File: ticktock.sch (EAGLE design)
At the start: 64 parts, among them IC1 ATMEGA644A, IC2 AD8611RM, IC3 REF200U, J1 AVR_SPI_PRG_6NS, Q1 MOSFET-NCHANNEL2N7002PW, Q2 MOSFET-NCHANNELBSS138, Q3 MOSFET-NCHANNELBSS138, U1 MAX232SOIC16, U2 OSCILLATORSMD, U3 FT232RLSSOP, U4 BMP180

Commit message: Fix ERC and DRC complaints.  Connect accidentally unconnected nets.
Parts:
- JP2: value (none) -> 3 Pin
- JP8: value (none) -> 7-Pin
- JP9: value (none) -> 3-Pin
- U$1: value (none) -> OPA381
- X1: value (none) -> RS232
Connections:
- net GND: now also U$1.IN+, U$1.V-

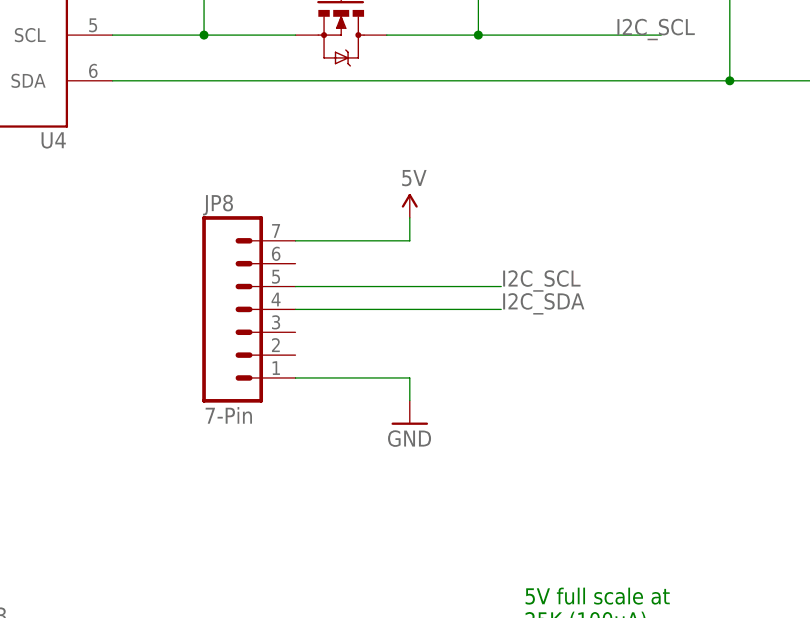
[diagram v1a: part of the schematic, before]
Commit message: Remove BMP carrier board header and Pull RS232 connector back to PCB edge
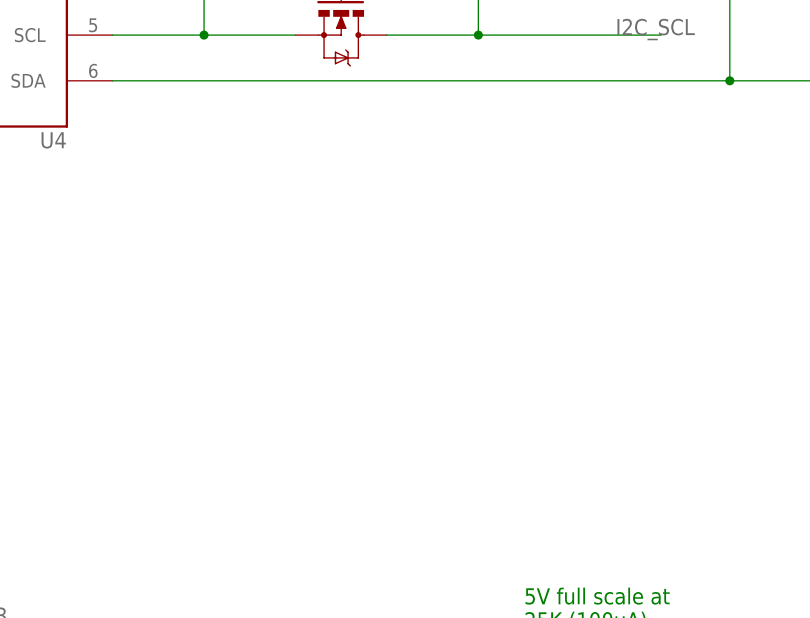
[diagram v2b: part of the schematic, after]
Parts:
- removed JP8: 7-Pin, SparkFun-Connectors:M07LOCK
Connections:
- net 5V: no longer JP8.7
- net GND: no longer JP8.1
- net I2C_SCL: no longer JP8.5
- net I2C_SDA: no longer JP8.4
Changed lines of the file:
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@@
 <part name="JP6" library="SparkFun-Connectors" deviceset="M01" device="PTH"/>
 <part name="JP7" library="SparkFun-Connectors" deviceset="M01" device="PTH"/>
-<part name="JP8" library="SparkFun-Connectors" deviceset="M07" device="LOCK" value="7-Pin"/>
-<part name="SUPPLY31" library="SparkFun-Aesthetics" deviceset="5V" device=""/>
-<part name="GND25" library="SparkFun-Aesthetics" deviceset="GND" device=""/>
 <part name="STANDOFF1" library="SparkFun-Electromechanical" deviceset="STAND-OFF" device=""/>
 <part name="STANDOFF2" library="SparkFun-Electromechanical" deviceset="STAND-OFF" device=""/>
@@
 <instance part="JP6" gate="G$1" x="200.66" y="198.12" rot="R270"/>
 <instance part="JP7" gate="G$1" x="190.5" y="198.12" rot="R270"/>
-<instance part="JP8" gate="G$1" x="403.86" y="111.76"/>
-<instance part="SUPPLY31" gate="G$1" x="421.64" y="124.46"/>
-<instance part="GND25" gate="1" x="421.64" y="101.6"/>
 <instance part="STANDOFF1" gate="G$1" x="487.68" y="307.34"/>
 <instance part="STANDOFF2" gate="G$1" x="487.68" y="302.26"/>
@@
 </segment>
 <segment>
-<pinref part="JP8" gate="G$1" pin="1"/>
-<wire x1="408.94" y1="106.68" x2="421.64" y2="106.68" width="0.1524" layer="91"/>
-<pinref part="GND25" gate="1" pin="GND"/>
-<wire x1="421.64" y1="106.68" x2="421.64" y2="104.14" width="0.1524" layer="91"/>
-</segment>
-<segment>
 <pinref part="U$1" gate="G$1" pin="IN+"/>
 <pinref part="GND21" gate="1" pin="GND"/>
@@
 <pinref part="SUPPLY27" gate="G$1" pin="5V"/>
 <wire x1="487.68" y1="160.02" x2="487.68" y2="180.34" width="0.1524" layer="91"/>
-</segment>
-<segment>
-<pinref part="JP8" gate="G$1" pin="7"/>
-<wire x1="408.94" y1="121.92" x2="421.64" y2="121.92" width="0.1524" layer="91"/>
-<pinref part="SUPPLY31" gate="G$1" pin="5V"/>
-<wire x1="421.64" y1="121.92" x2="421.64" y2="124.46" width="0.1524" layer="91"/>
 </segment>
 <segment>
@@
 <label x="187.96" y="124.46" size="1.778" layer="95"/>
 </segment>
-<segment>
-<pinref part="JP8" gate="G$1" pin="5"/>
-<wire x1="408.94" y1="116.84" x2="431.8" y2="116.84" width="0.1524" layer="91"/>
-<label x="431.8" y="116.84" size="1.778" layer="95"/>
-</segment>
 </net>
 <net name="N$18" class="0">
@@
 <label x="187.96" y="127" size="1.778" layer="95"/>
 </segment>
-<segment>
-<pinref part="JP8" gate="G$1" pin="4"/>
-<wire x1="408.94" y1="114.3" x2="431.8" y2="114.3" width="0.1524" layer="91"/>
-<label x="431.8" y="114.3" size="1.778" layer="95"/>
-</segment>
-</net>
+</net>

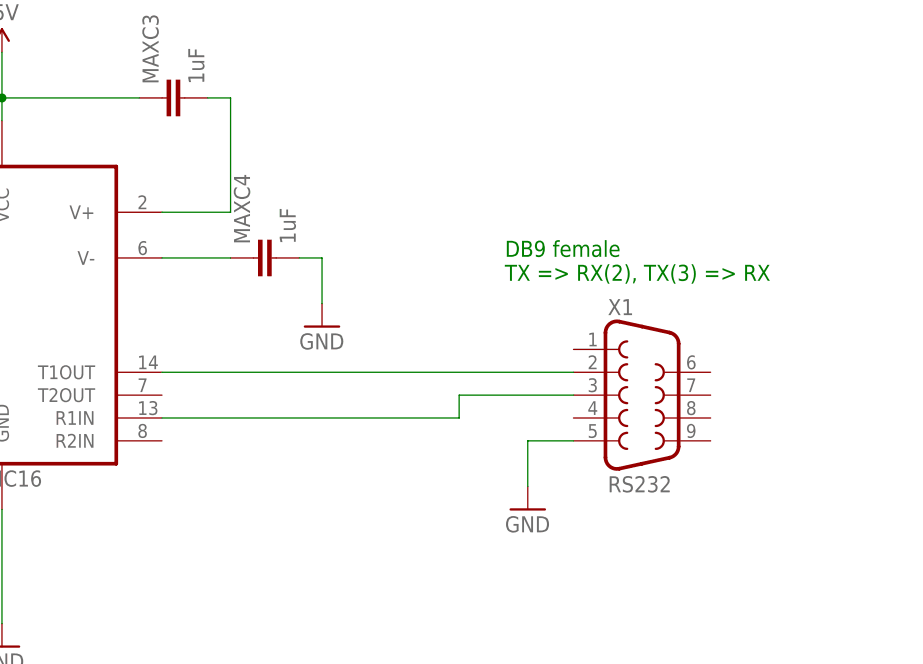
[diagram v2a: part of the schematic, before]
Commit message: Replace DB9 female connector with a male one
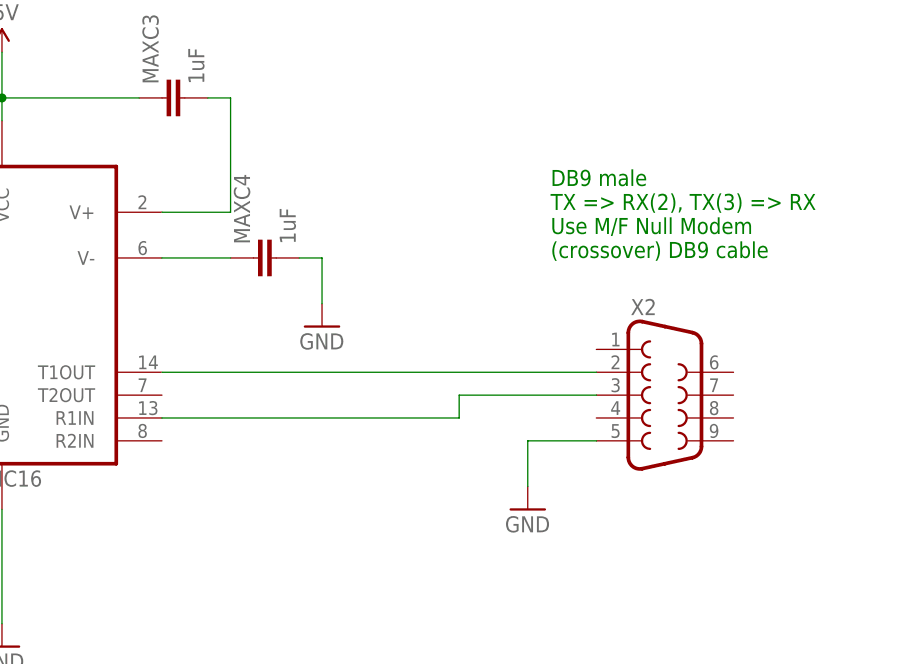
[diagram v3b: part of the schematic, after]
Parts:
- removed X1: RS232, SparkFun-Connectors:DB9FEMALE
- added X2: (no value), SparkFun-Connectors:DB9MALE
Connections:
- net GND: now also X2.5; no longer X1.5
- net N$10: now also X2.3; no longer X1.3
- net N$8: now also X2.2; no longer X1.2
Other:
- note added: "DB9 male TX => RX(2), TX(3) => RX Use M/F Null Modem (crossover) DB9 cable"
- note removed: "DB9 female TX => RX(2), TX(3) => RX"
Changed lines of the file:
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@@
 <part name="MAXC4" library="SparkFun-Capacitors" deviceset="CAP" device="0805" value="1uF"/>
 <part name="GND5" library="SparkFun-Aesthetics" deviceset="GND" device=""/>
-<part name="X1" library="SparkFun-Connectors" deviceset="DB9" device="FEMALE" value="RS232"/>
 <part name="GND6" library="SparkFun-Aesthetics" deviceset="GND" device=""/>
 <part name="GPS_10MHZ_IN" library="SparkFun-Connectors" deviceset="BNC" device="PTH"/>
@@
 <part name="STANDOFF4" library="SparkFun-Electromechanical" deviceset="STAND-OFF" device=""/>
 <part name="JP9" library="SparkFun-Connectors" deviceset="M03" device="LOCK" value="3-Pin"/>
+<part name="X2" library="SparkFun-Connectors" deviceset="DB9" device="MALE"/>
 </parts>
 <sheets>
@@
 <text x="403.86" y="358.14" size="1.778" layer="91">Only using one of the
 MAX232's Rx/Tx pairs</text>
-<text x="510.54" y="388.62" size="1.778" layer="91">DB9 female
+<text x="515.62" y="391.16" size="1.778" layer="91">DB9 male
 TX =&gt; RX(2), TX(3) =&gt; RX
-</text>
+Use M/F Null Modem
+(crossover) DB9 cable</text>
 <text x="20.32" y="40.64" size="1.778" layer="91">USB-B
 (square)</text>
@@
 </instance>
 <instance part="GND5" gate="1" x="490.22" y="383.54"/>
-<instance part="X1" gate="G$1" x="525.78" y="375.92"/>
 <instance part="GND6" gate="1" x="513.08" y="363.22"/>
 <instance part="GPS_10MHZ_IN" gate="G$1" x="307.34" y="327.66"/>
@@
 <instance part="STANDOFF4" gate="G$1" x="487.68" y="292.1"/>
 <instance part="JP9" gate="G$1" x="220.98" y="83.82" rot="R270"/>
+<instance part="X2" gate="G$1" x="528.32" y="375.92"/>
 </instances>
 <busses>
@@
 </segment>
 <segment>
-<pinref part="X1" gate="G$1" pin="5"/>
-<wire x1="518.16" y1="370.84" x2="513.08" y2="370.84" width="0.1524" layer="91"/>
+<wire x1="520.7" y1="370.84" x2="513.08" y2="370.84" width="0.1524" layer="91"/>
 <pinref part="GND6" gate="1" pin="GND"/>
 <wire x1="513.08" y1="370.84" x2="513.08" y2="365.76" width="0.1524" layer="91"/>
+<pinref part="X2" gate="G$1" pin="5"/>
 </segment>
 <segment>
@@
 <segment>
 <pinref part="U1" gate="G$1" pin="T1OUT"/>
-<wire x1="472.44" y1="378.46" x2="518.16" y2="378.46" width="0.1524" layer="91"/>
-<pinref part="X1" gate="G$1" pin="2"/>
+<wire x1="472.44" y1="378.46" x2="520.7" y2="378.46" width="0.1524" layer="91"/>
+<pinref part="X2" gate="G$1" pin="2"/>
 </segment>
 </net>
@@
 <wire x1="472.44" y1="373.38" x2="505.46" y2="373.38" width="0.1524" layer="91"/>
 <wire x1="505.46" y1="373.38" x2="505.46" y2="375.92" width="0.1524" layer="91"/>
-<pinref part="X1" gate="G$1" pin="3"/>
-<wire x1="505.46" y1="375.92" x2="518.16" y2="375.92" width="0.1524" layer="91"/>
-</segment>
-</net>
+<wire x1="505.46" y1="375.92" x2="520.7" y2="375.92" width="0.1524" layer="91"/>
+<pinref part="X2" gate="G$1" pin="3"/>
+</segment>
+</net>

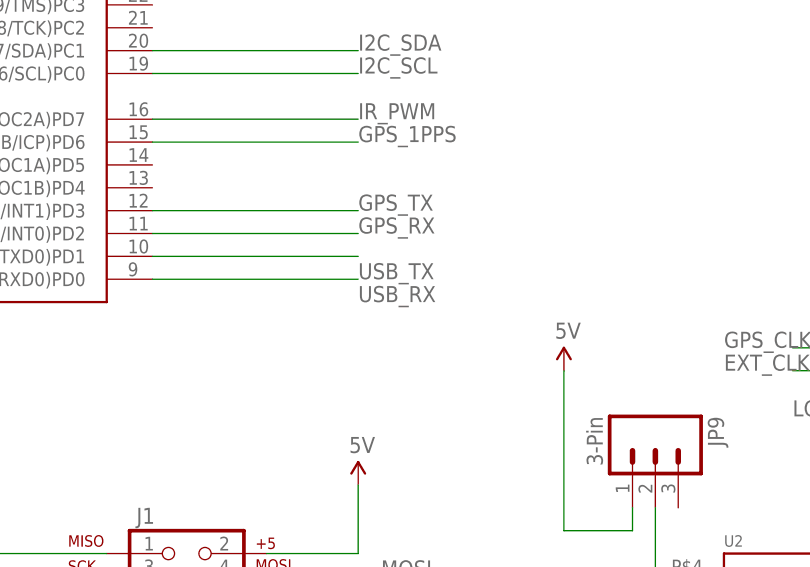
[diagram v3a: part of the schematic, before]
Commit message: Flip USB_TX and USB_RX in schematic
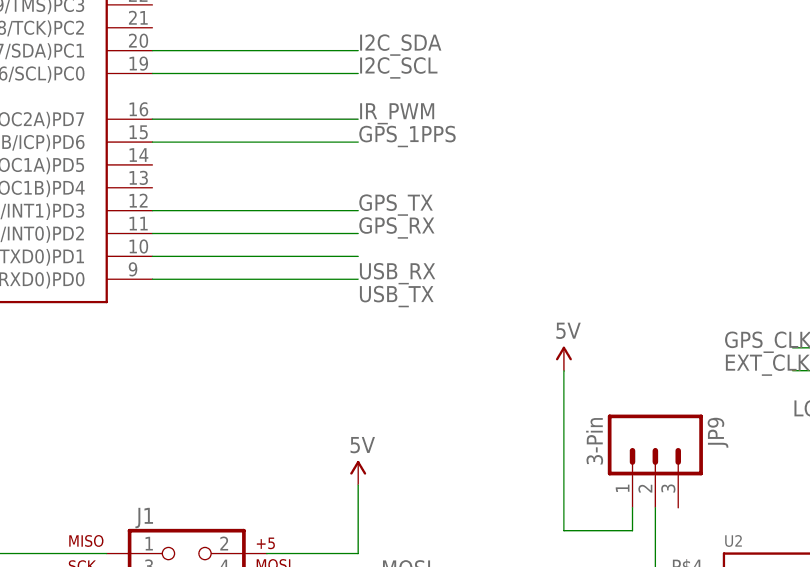
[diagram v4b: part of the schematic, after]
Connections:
- net USB_RX: now also IC1.(PCINT25/TXD0)PD1; no longer IC1.(PCINT24/RXD0)PD0
- net USB_TX: now also IC1.(PCINT24/RXD0)PD0; no longer IC1.(PCINT25/TXD0)PD1
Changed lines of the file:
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@@
+</segment>
+</net>
+<net name="USB_RX" class="0">
+<segment>
+<pinref part="IC1" gate="G$1" pin="(PCINT25/TXD0)PD1"/>
+<wire x1="165.1" y1="104.14" x2="187.96" y2="104.14" width="0.1524" layer="91"/>
+<label x="187.96" y="101.6" size="1.778" layer="95"/>
+</segment>
+<segment>
+<pinref part="U3" gate="G$1" pin="RXD"/>
+<wire x1="88.9" y1="58.42" x2="101.6" y2="58.42" width="0.1524" layer="91"/>
+<label x="101.6" y="58.42" size="1.778" layer="95"/>
 </segment>
 </net>
 <net name="USB_TX" class="0">
+<segment>
+<pinref part="IC1" gate="G$1" pin="(PCINT24/RXD0)PD0"/>
+<wire x1="165.1" y1="101.6" x2="187.96" y2="101.6" width="0.1524" layer="91"/>
+<label x="187.96" y="99.06" size="1.778" layer="95"/>
+</segment>
 <segment>
 <pinref part="U3" gate="G$1" pin="TXD"/>
@@
 <label x="101.6" y="60.96" size="1.778" layer="95"/>
 </segment>
-<segment>
-<pinref part="IC1" gate="G$1" pin="(PCINT25/TXD0)PD1"/>
-<wire x1="165.1" y1="104.14" x2="187.96" y2="104.14" width="0.1524" layer="91"/>
-<label x="187.96" y="101.6" size="1.778" layer="95"/>
-</segment>
 </net>
-<net name="USB_RX" class="0">
-<segment>
-<pinref part="U3" gate="G$1" pin="RXD"/>
-<wire x1="88.9" y1="58.42" x2="101.6" y2="58.42" width="0.1524" layer="91"/>
-<label x="101.6" y="58.42" size="1.778" layer="95"/>
-</segment>
-<segment>
-<pinref part="IC1" gate="G$1" pin="(PCINT24/RXD0)PD0"/>
-<wire x1="165.1" y1="101.6" x2="187.96" y2="101.6" width="0.1524" layer="91"/>
-<label x="187.96" y="99.06" size="1.778" layer="95"/>
-</segment>
-</net>

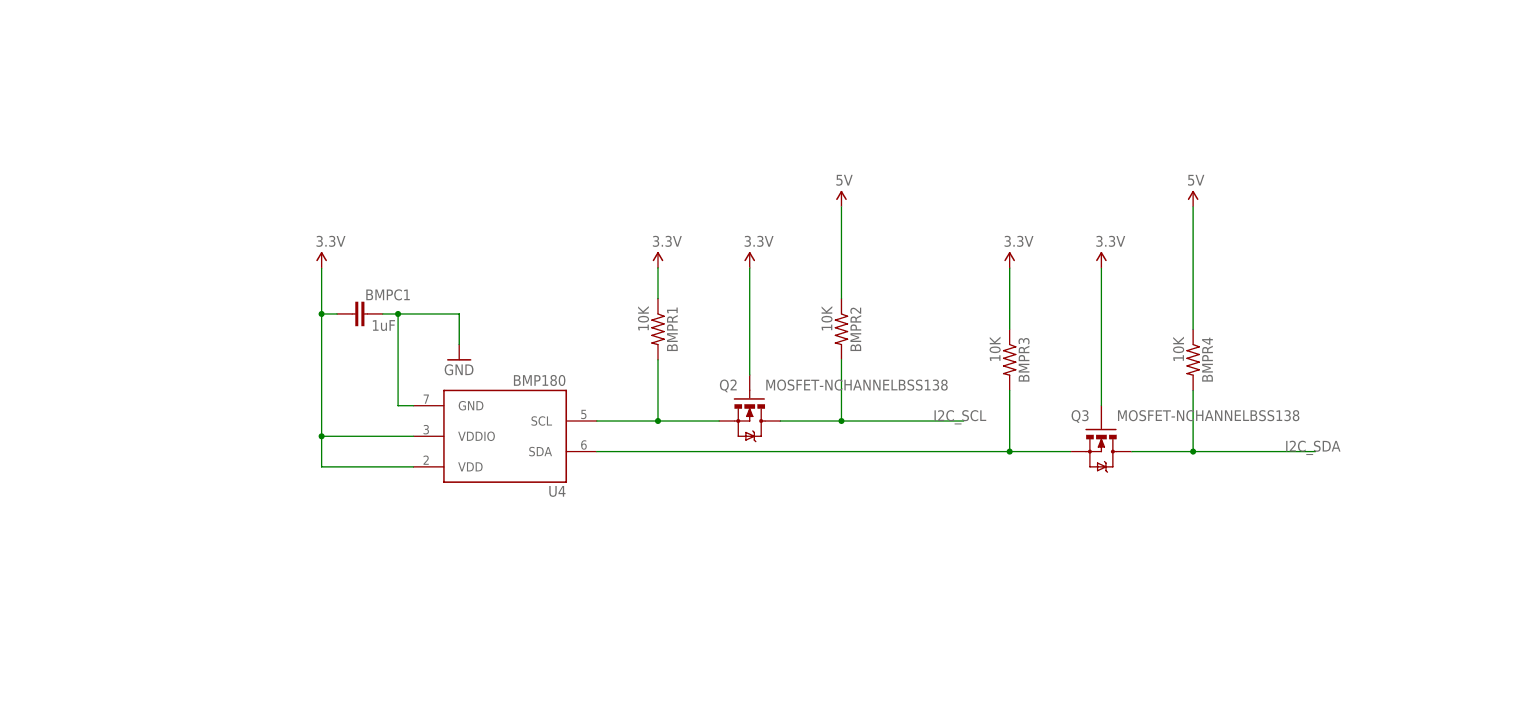
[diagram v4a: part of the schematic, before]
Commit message: Drop in BME280 (remove BMP180)
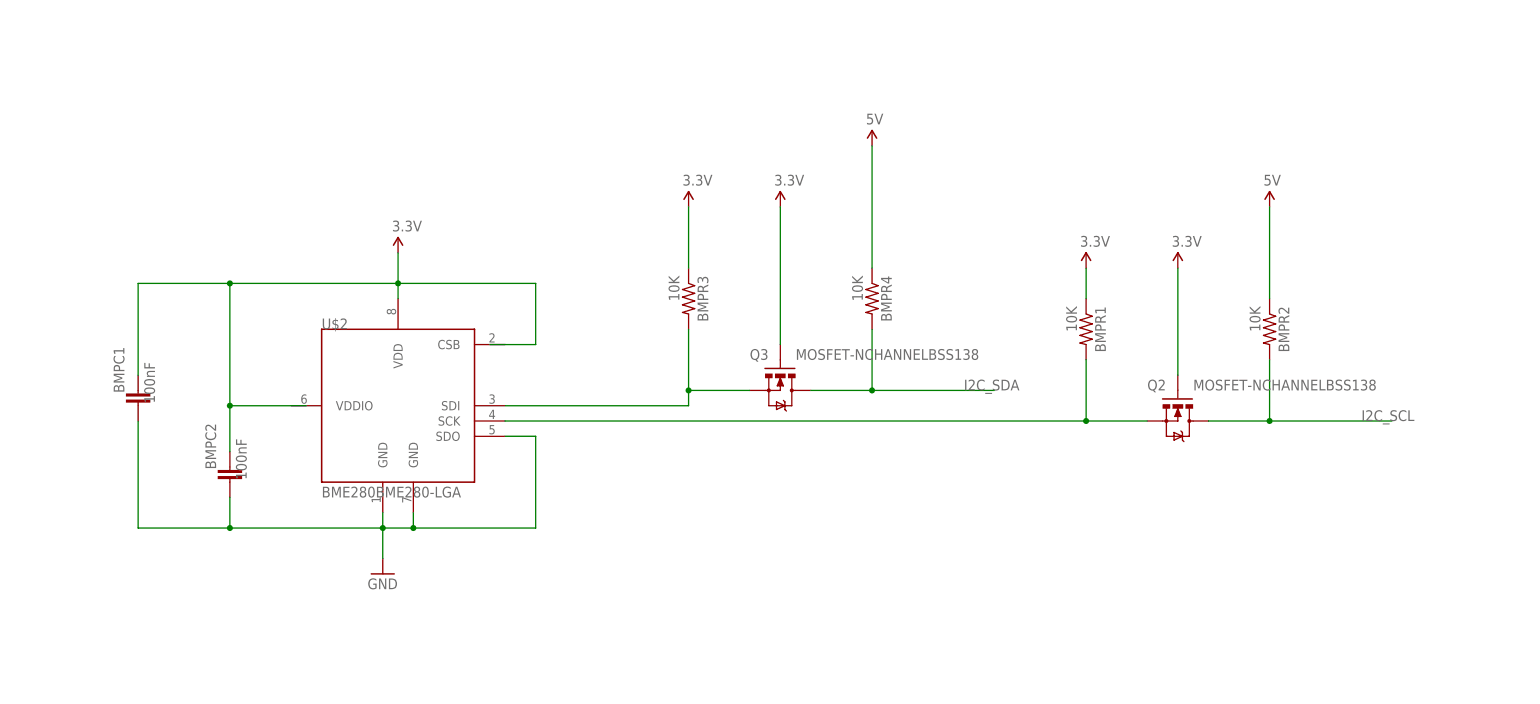
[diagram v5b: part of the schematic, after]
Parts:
- removed U4: BMP180, SparkFun-Sensors:BMP180
- added BMPC2: 100nF, SparkFun-Capacitors:CAP0805
- added U$2: BME280BME280-LGA, tickTockLibrary:BME280BME280-LGA
- BMPC1: value 1uF -> 100nF
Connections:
- net 3.3V: now also BMPC1.2, BMPC2.2, U$2.VDD; no longer BMPC1.1, U4.VDD, U4.VDDIO
- net GND: now also BMPC1.1, BMPC2.1, U$2.GND@1, U$2.GND@2, U$2.SDO; no longer BMPC1.2, U4.GND
- net N$15: now also U$2.SCK; no longer U4.SCL
- net N$18: now also U$2.SDI; no longer U4.SDA
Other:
- moved on the sheet: BMPC1, BMPR1, BMPR2, BMPR3, BMPR4, Q2, Q3
